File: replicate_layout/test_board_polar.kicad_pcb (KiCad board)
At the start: 2 copper layers, 30 parts, among them J1001 Pusa_4mm, J1002 Pusa_4mm, Q1001 CSD19531KCS, Q1002 CSD19531KCS, Q1003 CSD19531KCS, Q2001 CSD19531KCS, Q2002 CSD19531KCS, Q3001 CSD19531KCS, Q3002 CSD19531KCS, Q4001 CSD19531KCS, Q4002 CSD19531KCS, U1001 LAUNCHXL-F28377S, U2001 IR2181, U3001 IR2181, U4001 IR2181

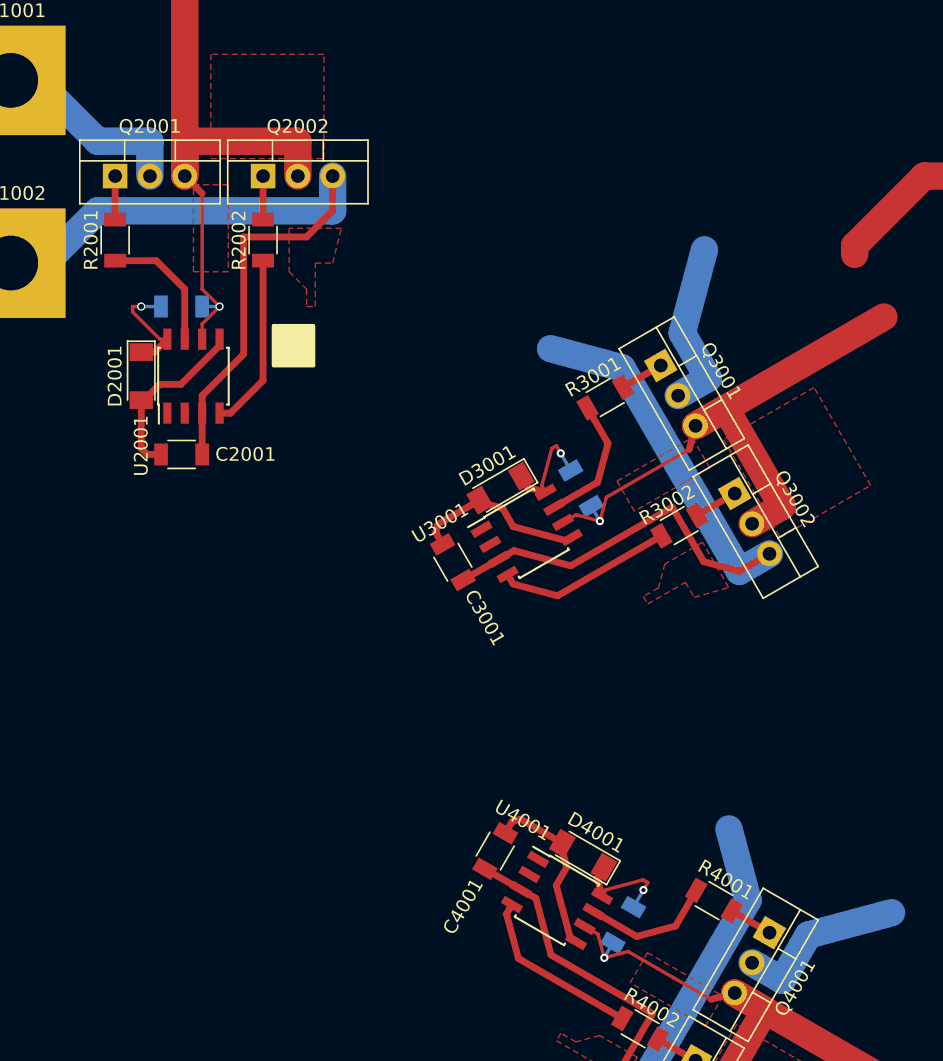
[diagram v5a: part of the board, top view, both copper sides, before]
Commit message: Added replication of tracks which are outside of bounding box but are on nets which are contained only within the sheet to be replicated.
updated test layouts.
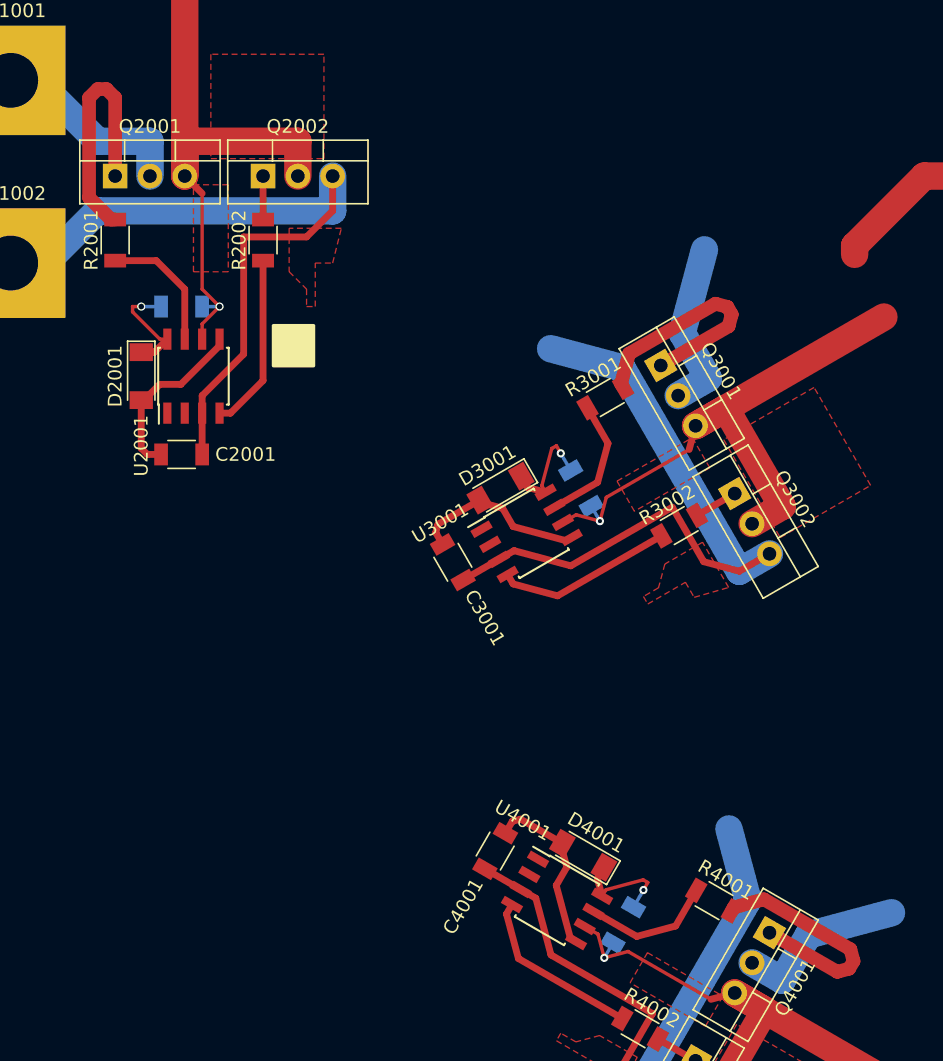
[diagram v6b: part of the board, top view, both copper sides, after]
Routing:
- net /Veja_1/QH_G: track 3.17 -> 18.0 mm
- net /Veja_2/QH_G: track 3.18 -> 18.0 mm
- net /Veja_3/QH_G: track 3.18 -> 18.0 mm
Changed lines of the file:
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@@
     (thickness 1.6)
     (drawings 0)
-    (tracks 149)
+    (tracks 167)
     (zones 0)
     (modules 30)
@@
       (effects (font (size 1 1) (thickness 0.15)))
     )
-    (pad 8 smd rect (at 2.7 -1.904999 30) (size 1.55 0.6) (layers F.Cu F.Paste F.Mask)
+    (pad 8 smd rect (at 2.7 -1.905 30) (size 1.55 0.6) (layers F.Cu F.Paste F.Mask)
       (net 11 "Net-(C3002-Pad1)"))
     (pad 7 smd rect (at 2.7 -0.635 30) (size 1.55 0.6) (layers F.Cu F.Paste F.Mask)
@@
     (pad 6 smd rect (at 2.7 0.635 30) (size 1.55 0.6) (layers F.Cu F.Paste F.Mask)
       (net 4 /Veja_2/OUT))
-    (pad 5 smd rect (at 2.700001 1.905 30) (size 1.55 0.6) (layers F.Cu F.Paste F.Mask)
+    (pad 5 smd rect (at 2.7 1.905 30) (size 1.55 0.6) (layers F.Cu F.Paste F.Mask)
       (net 1 +12V))
-    (pad 4 smd rect (at -2.7 1.904999 30) (size 1.55 0.6) (layers F.Cu F.Paste F.Mask)
+    (pad 4 smd rect (at -2.7 1.905 30) (size 1.55 0.6) (layers F.Cu F.Paste F.Mask)
       (net 26 /Veja_2/test/zaj))
     (pad 3 smd rect (at -2.7 0.635 30) (size 1.55 0.6) (layers F.Cu F.Paste F.Mask)
@@
     (pad 2 smd rect (at -2.7 -0.635 30) (size 1.55 0.6) (layers F.Cu F.Paste F.Mask)
       (net 9 /Veja_2/LIN))
-    (pad 1 smd rect (at -2.700001 -1.905 30) (size 1.55 0.6) (layers F.Cu F.Paste F.Mask)
+    (pad 1 smd rect (at -2.7 -1.905 30) (size 1.55 0.6) (layers F.Cu F.Paste F.Mask)
       (net 8 /Veja_2/HIN))
     (model ${KISYS3DMOD}/Housings_SOIC.3dshapes/SOIC-8_3.9x4.9mm_Pitch1.27mm.wrl
@@
       (effects (font (size 1 1) (thickness 0.15)))
     )
-    (pad 8 smd rect (at 2.700001 -1.905 330) (size 1.55 0.6) (layers F.Cu F.Paste F.Mask)
+    (pad 8 smd rect (at 2.7 -1.905 330) (size 1.55 0.6) (layers F.Cu F.Paste F.Mask)
       (net 12 "Net-(C4002-Pad1)"))
     (pad 7 smd rect (at 2.7 -0.635 330) (size 1.55 0.6) (layers F.Cu F.Paste F.Mask)
@@
     (pad 6 smd rect (at 2.7 0.635 330) (size 1.55 0.6) (layers F.Cu F.Paste F.Mask)
       (net 13 /Veja_3/OUT))
-    (pad 5 smd rect (at 2.7 1.904999 330) (size 1.55 0.6) (layers F.Cu F.Paste F.Mask)
+    (pad 5 smd rect (at 2.7 1.905 330) (size 1.55 0.6) (layers F.Cu F.Paste F.Mask)
       (net 1 +12V))
-    (pad 4 smd rect (at -2.700001 1.905 330) (size 1.55 0.6) (layers F.Cu F.Paste F.Mask)
+    (pad 4 smd rect (at -2.7 1.905 330) (size 1.55 0.6) (layers F.Cu F.Paste F.Mask)
       (net 27 /Veja_3/test/zaj))
     (pad 3 smd rect (at -2.7 0.635 330) (size 1.55 0.6) (layers F.Cu F.Paste F.Mask)
@@
     (pad 2 smd rect (at -2.7 -0.635 330) (size 1.55 0.6) (layers F.Cu F.Paste F.Mask)
       (net 18 /Veja_3/LIN))
-    (pad 1 smd rect (at -2.7 -1.904999 330) (size 1.55 0.6) (layers F.Cu F.Paste F.Mask)
+    (pad 1 smd rect (at -2.7 -1.905 330) (size 1.55 0.6) (layers F.Cu F.Paste F.Mask)
       (net 17 /Veja_3/HIN))
     (model ${KISYS3DMOD}/Housings_SOIC.3dshapes/SOIC-8_3.9x4.9mm_Pitch1.27mm.wrl
@@
   (segment (start 212.909495 147.847169) (end 205.327443 143.469669) (width 0.5) (layer F.Cu) (net 27))
   (segment (start 218.257202 150.934669) (end 215.507571 149.347169) (width 0.5) (layer F.Cu) (net 24))
-  (segment (start 223.654702 141.585924) (end 220.905071 139.998424) (width 0.5) (layer F.Cu) (net 23))
+  (segment (start 221.055071 139.738617) (end 223.247542 139.151146) (width 1) (layer F.Cu) (net 23))
+  (segment (start 220.905071 139.998424) (end 221.055071 139.738617) (width 1) (layer F.Cu) (net 23))
+  (segment (start 223.247542 139.151146) (end 229.556537 142.793646) (width 1) (layer F.Cu) (net 23))
+  (segment (start 229.556537 142.793646) (end 229.788963 143.661072) (width 1) (layer F.Cu) (net 23))
+  (segment (start 229.788963 143.661072) (end 229.471463 144.210998) (width 1) (layer F.Cu) (net 23))
+  (segment (start 228.604037 144.443424) (end 223.654702 141.585924) (width 1) (layer F.Cu) (net 23))
+  (segment (start 229.471463 144.210998) (end 228.604037 144.443424) (width 1) (layer F.Cu) (net 23))
   (segment (start 210.80467 140.032833) (end 213.965662 141.857833) (width 0.5) (layer F.Cu) (net 16))
   (segment (start 216.806995 141.096501) (end 218.306995 138.498424) (width 0.5) (layer F.Cu) (net 16))
@@
   (segment (start 215.766995 112.622168) (end 208.184943 116.999668) (width 0.5) (layer F.Cu) (net 26))
   (segment (start 221.114702 109.534668) (end 218.365071 111.122168) (width 0.5) (layer F.Cu) (net 22))
-  (segment (start 215.717202 100.185923) (end 212.967571 101.773423) (width 0.5) (layer F.Cu) (net 21))
+  (segment (start 212.817571 101.513616) (end 213.405042 99.321145) (width 1) (layer F.Cu) (net 21))
+  (segment (start 212.967571 101.773423) (end 212.817571 101.513616) (width 1) (layer F.Cu) (net 21))
+  (segment (start 213.405042 99.321145) (end 219.714037 95.678645) (width 1) (layer F.Cu) (net 21))
+  (segment (start 219.714037 95.678645) (end 220.581463 95.911071) (width 1) (layer F.Cu) (net 21))
+  (segment (start 220.581463 95.911071) (end 220.898963 96.460997) (width 1) (layer F.Cu) (net 21))
+  (segment (start 220.666537 97.328423) (end 215.717202 100.185923) (width 1) (layer F.Cu) (net 21))
+  (segment (start 220.898963 96.460997) (end 220.666537 97.328423) (width 1) (layer F.Cu) (net 21))
   (segment (start 207.94717 110.537832) (end 211.108162 108.712832) (width 0.5) (layer F.Cu) (net 15))
   (segment (start 211.869495 105.8715) (end 210.369495 103.273423) (width 0.5) (layer F.Cu) (net 15))
@@
   (segment (start 178.895 92.535) (end 175.895 92.535) (width 0.5) (layer F.Cu) (net 14))
   (segment (start 180.975 98.265) (end 180.975 94.615) (width 0.5) (layer F.Cu) (net 14))
-  (segment (start 175.895 86.36) (end 175.895 89.535) (width 0.5) (layer F.Cu) (net 19))
+  (segment (start 175.26 80.01) (end 175.895 80.645) (width 1) (layer F.Cu) (net 19))
+  (segment (start 175.895 80.645) (end 175.895 86.36) (width 1) (layer F.Cu) (net 19))
+  (segment (start 174.625 80.01) (end 175.26 80.01) (width 1) (layer F.Cu) (net 19))
+  (segment (start 173.99 80.645) (end 174.625 80.01) (width 1) (layer F.Cu) (net 19))
+  (segment (start 173.99 87.93) (end 173.99 80.645) (width 1) (layer F.Cu) (net 19))
+  (segment (start 175.895 89.535) (end 175.595 89.535) (width 1) (layer F.Cu) (net 19))
+  (segment (start 175.595 89.535) (end 173.99 87.93) (width 1) (layer F.Cu) (net 19))
   (segment (start 186.69 86.36) (end 186.69 89.535) (width 0.5) (layer F.Cu) (net 20))
   (segment (start 186.69 92.535) (end 186.69 101.29) (width 0.5) (layer F.Cu) (net 25))
